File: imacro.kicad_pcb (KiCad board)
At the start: 2 copper layers, 57.2 x 83.3 mm, 28 parts, among them SW0:0 Choc, SW0:1 Choc, SW0:2 Choc, SW1:0 Choc, SW1:1 Choc, SW1:2 Choc, SW2:0 Choc, SW2:1 Choc, SW2:2 Choc, SW3:0 Choc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

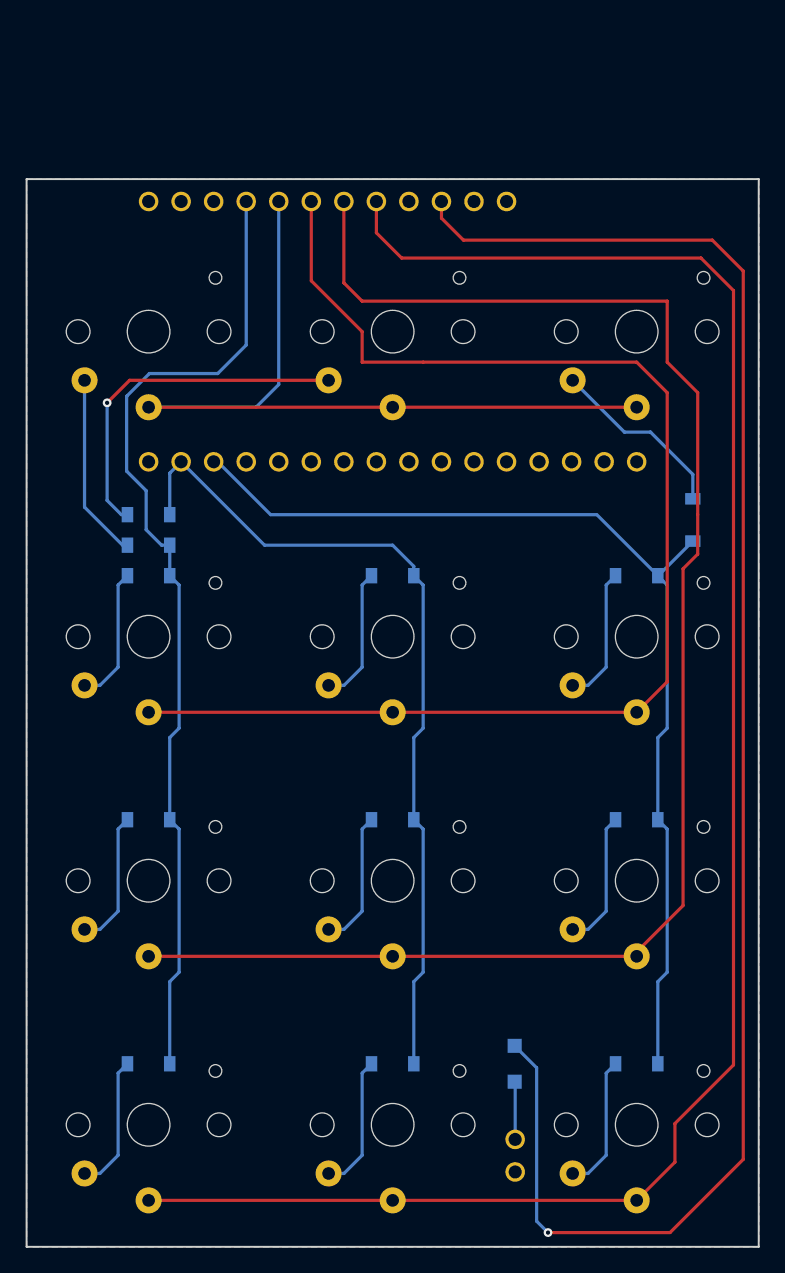
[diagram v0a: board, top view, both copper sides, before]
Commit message: Finish PCB layout; add necessary footprints to library; adjust pad drill size for key switches
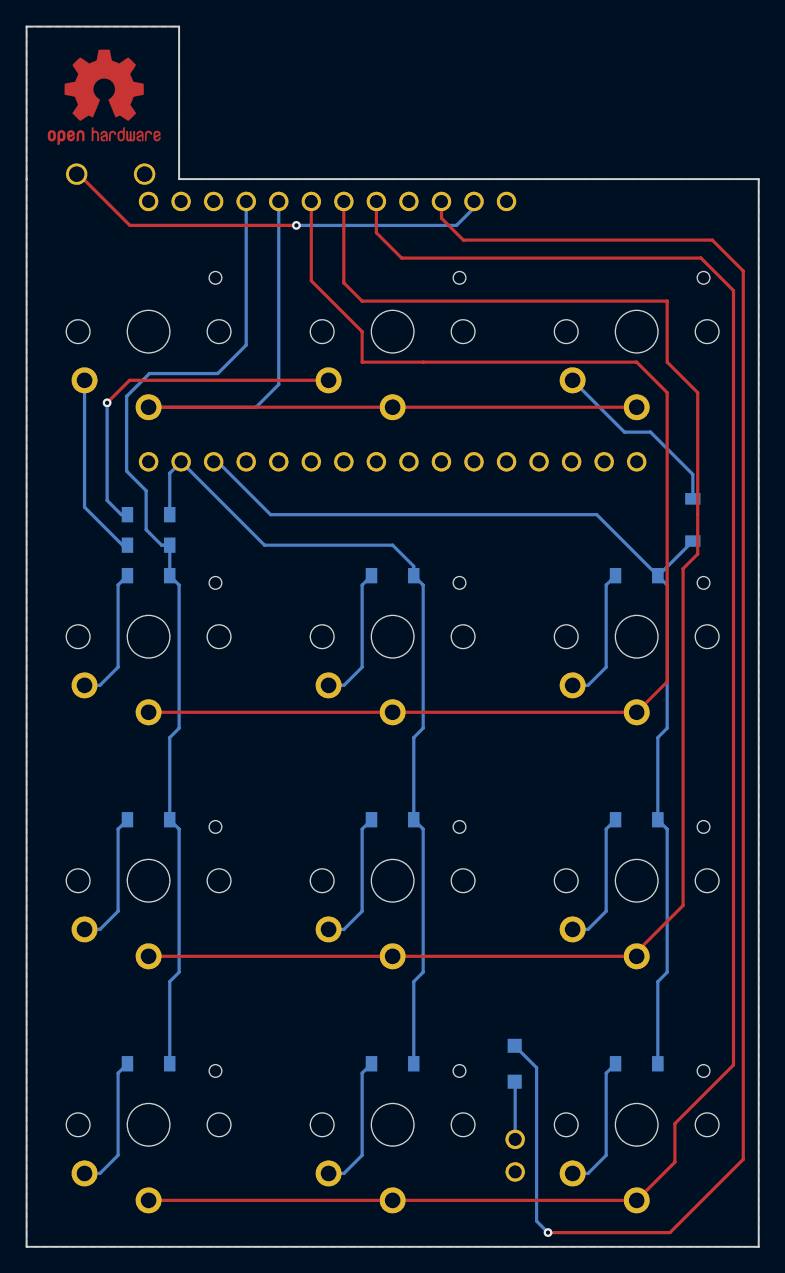
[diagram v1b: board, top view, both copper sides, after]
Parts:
- removed the REF*** at (90.4, 116.3)
- added REF***: OSHW-Logo2_9.8x8mm_Copper, Symbols:OSHW-Logo2_9.8x8mm_Copper, F.Cu at (77.5, 46.0)
- added SW1: TOGGLE, imacro:GPTS_SPST_Pushbutton, B.Cu at (78.0, 46.0)
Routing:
- net Net-(SW1-Pad2): track 0.00 -> 33.7 mm, vias 0 -> 1
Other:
- board size 57.2 x 83.3 mm -> 57.2 x 95.2 mm
